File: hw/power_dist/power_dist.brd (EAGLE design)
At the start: 80 x 50 mm, 66 parts, among them J1 JST-ZH6SMT_VERT, J2 JST-PH4SMT_VERT, J3 JST-PH5VERT, P1 XT30P, P2 XT30P, P3 XT30P, P4 XT30P, P5 XT30P, P6 XT30P, P7 XT90PW-M, Q1 PSMN4R8-100BSEJ, Q2 PSMN4R8-100BSEJ, Q3 PSMN4R8-100BSEJ, Q4 MF-DSC-SOT233-BSS138, Q5 MF-DSC-SOT233-MMBT3906, U1 MAX15062AATA+T, U2 STM32G474CEU6, U3 LM5066IPMHE/NOPB, U4 TCAN334G

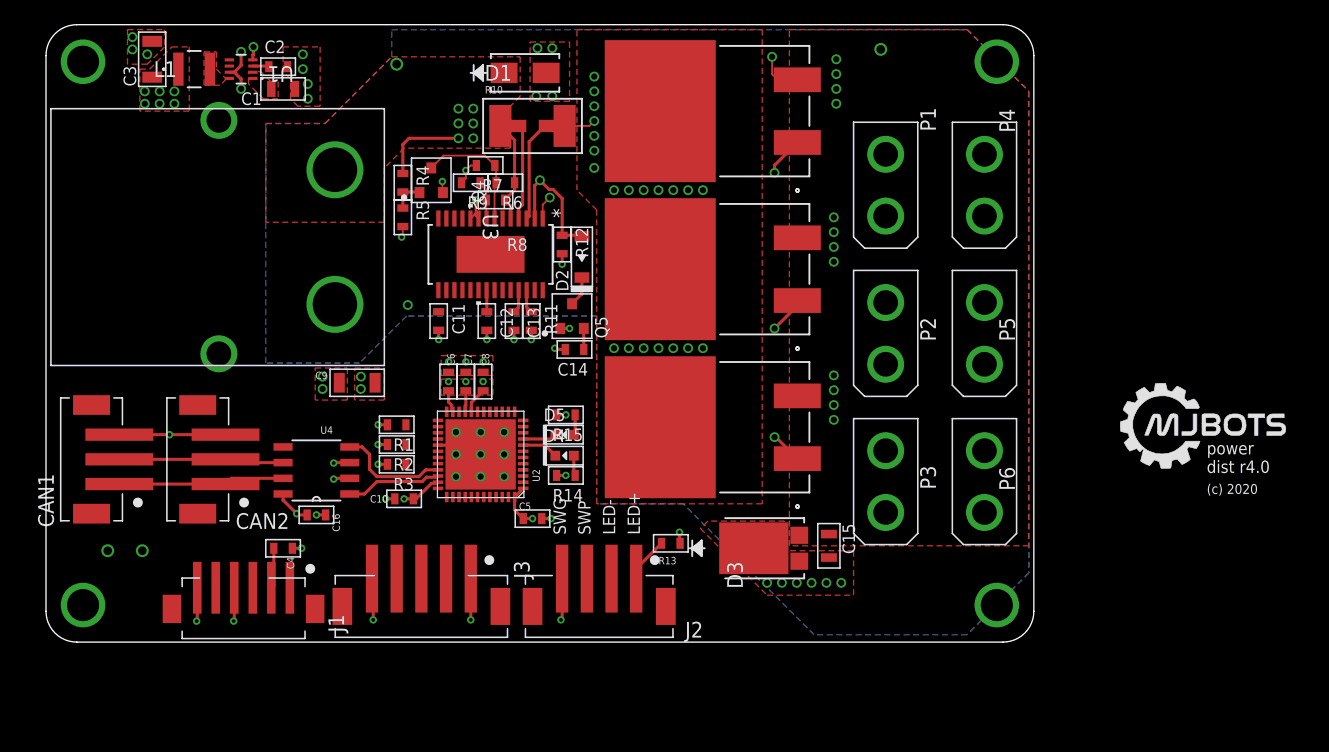
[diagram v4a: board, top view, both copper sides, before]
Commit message: power_dist r4: Resize and rough place silks
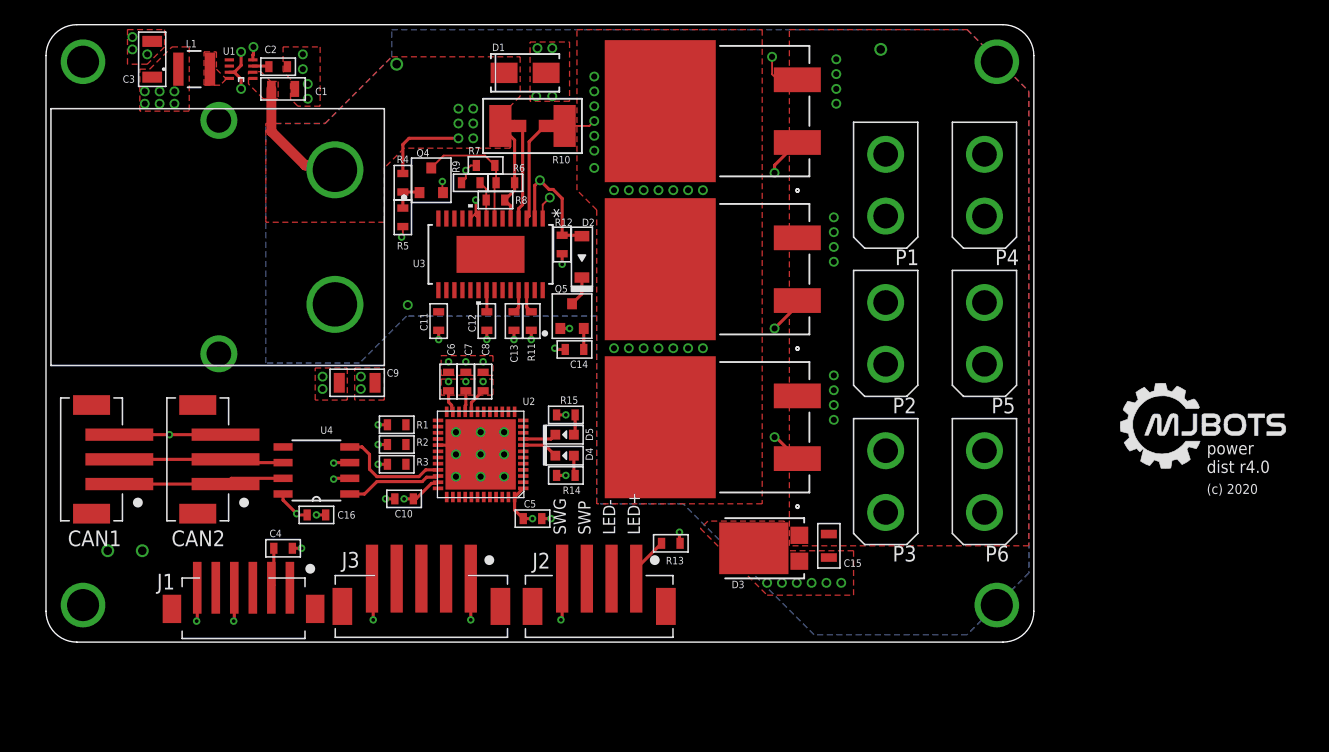
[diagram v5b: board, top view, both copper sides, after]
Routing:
- net +24V: track 15.6 -> 25.4 mm

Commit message: power_dist r4: Place logo
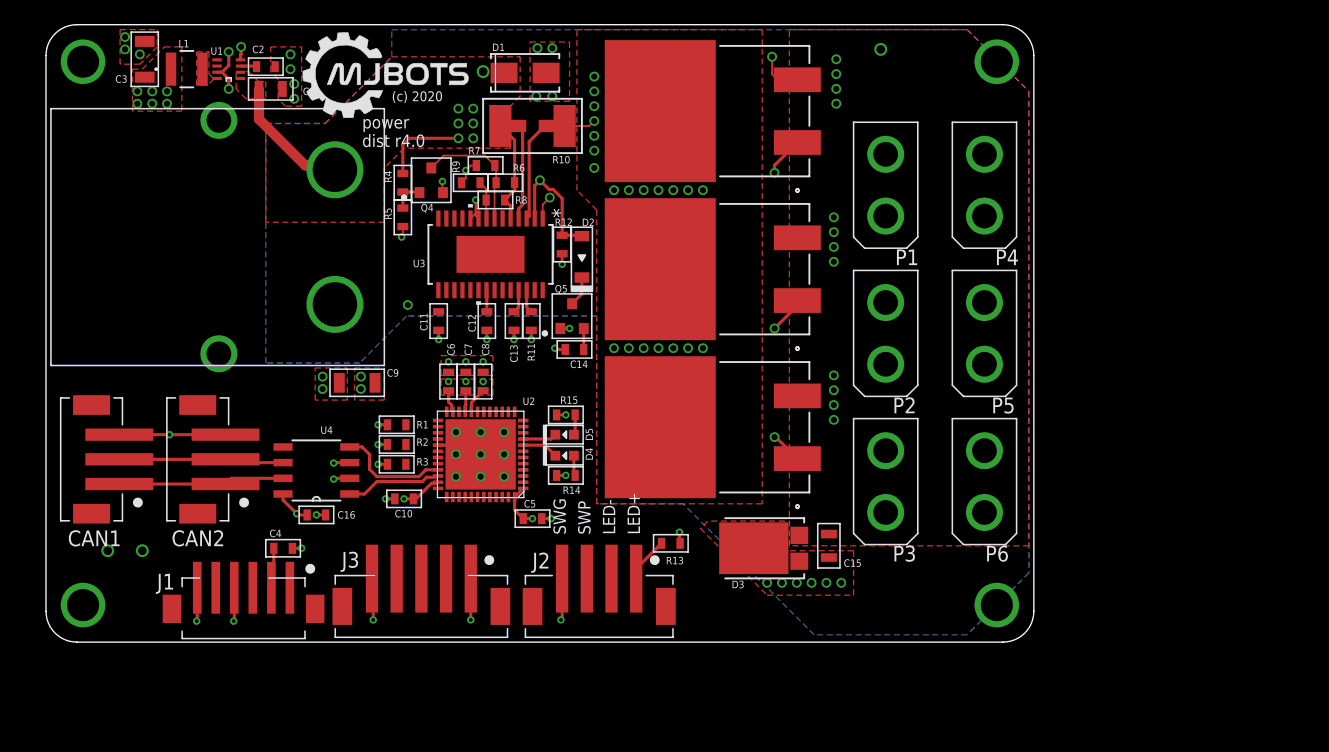
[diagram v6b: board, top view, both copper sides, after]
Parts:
- moved DB_VIN 7.03 mm to (35.4, 46.2)
- moved C1 1.00 mm to (18.2, 44.8)
- moved C2 1.00 mm to (17.8, 46.6)
- moved U1 1.00 mm to (14.8, 46.4)
- moved C3 0.60 mm to (8.00, 47.2)
- moved L1 0.60 mm to (11.4, 46.4)

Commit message: power_dist r4: Routed and labels
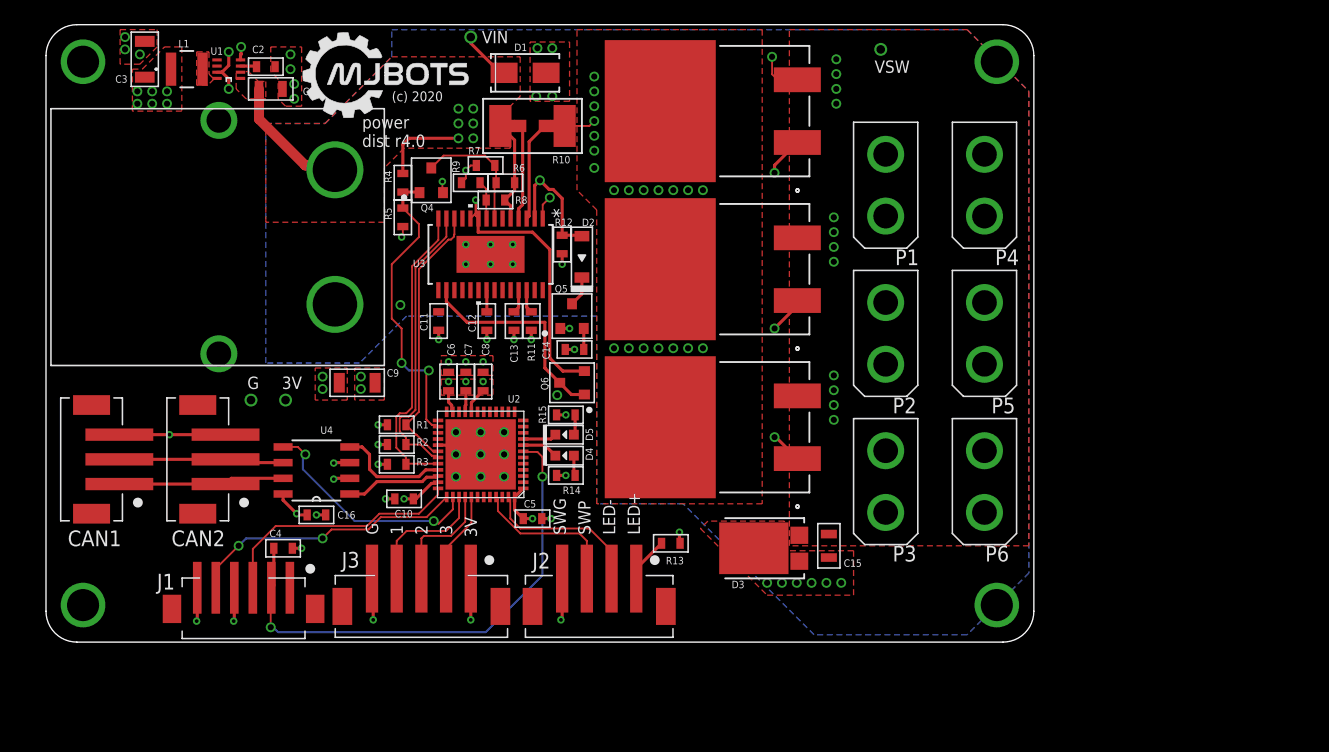
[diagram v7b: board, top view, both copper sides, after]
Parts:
- added Q6: MF-DSC-SOT233-MMBT3904, mfdiscretesemi:SOT-23-3
- moved DB_3 18.9 mm to (19.4, 19.6)
- moved DB_G 15.0 mm to (16.6, 19.6)
- moved DB_VIN 2.97 mm to (34.4, 49.0)
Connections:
- new net N$3: Q6.P$1, Q6.P$3, U3.16
- net CAN_SHDN: now also U2.38; no longer U2.27
- net GND: now also Q6.P$2
- net PWR_LED: now also U2.47; no longer U2.10
- net PWR_SW: now also U2.45; no longer U2.11
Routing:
- net NRST: track 3.28 -> 41.9 mm, vias 0 -> 2
- net SMBA: track 0.00 -> 24.6 mm
- net SCL: track 0.00 -> 23.5 mm
- net SWCLK: track 0.00 -> 22.7 mm, vias 0 -> 2
- net PSHDN: track 2.74 -> 24.9 mm, vias 0 -> 2
- net SDA: track 0.00 -> 21.9 mm
- net SWDIO: track 0.00 -> 20.5 mm
- net GND: track 43.0 -> 62.3 mm, vias 54 -> 60
- net CAN_SHDN: track 0.00 -> 18.8 mm, vias 0 -> 2
- net N$3: track 0.00 -> 17.4 mm
- net PWR_LED: track 0.00 -> 13.3 mm
- net PWR_SW: track 0.00 -> 12.5 mm
- net GPIO1: track 0.00 -> 10.6 mm
- net GPIO2: track 0.00 -> 9.37 mm
- net GPIO3: track 0.00 -> 7.46 mm
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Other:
- board text added: "1"
- board text added: "2"
- board text added: "3"
- board text added: "3V"
- board text added: "G"
- board text added: "VIN"
- board text added: "VSW"

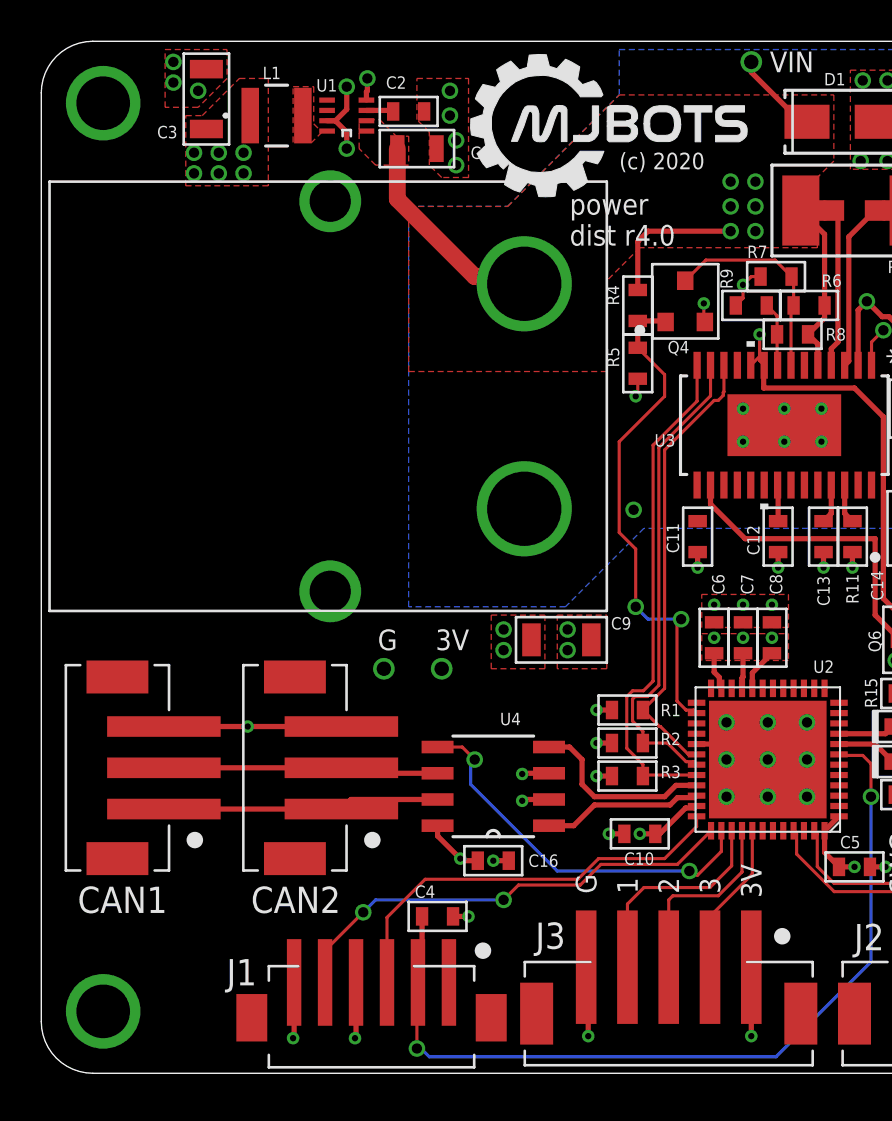
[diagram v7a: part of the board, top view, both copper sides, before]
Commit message: power_dist r4: Optionally ground one of the mounting holes
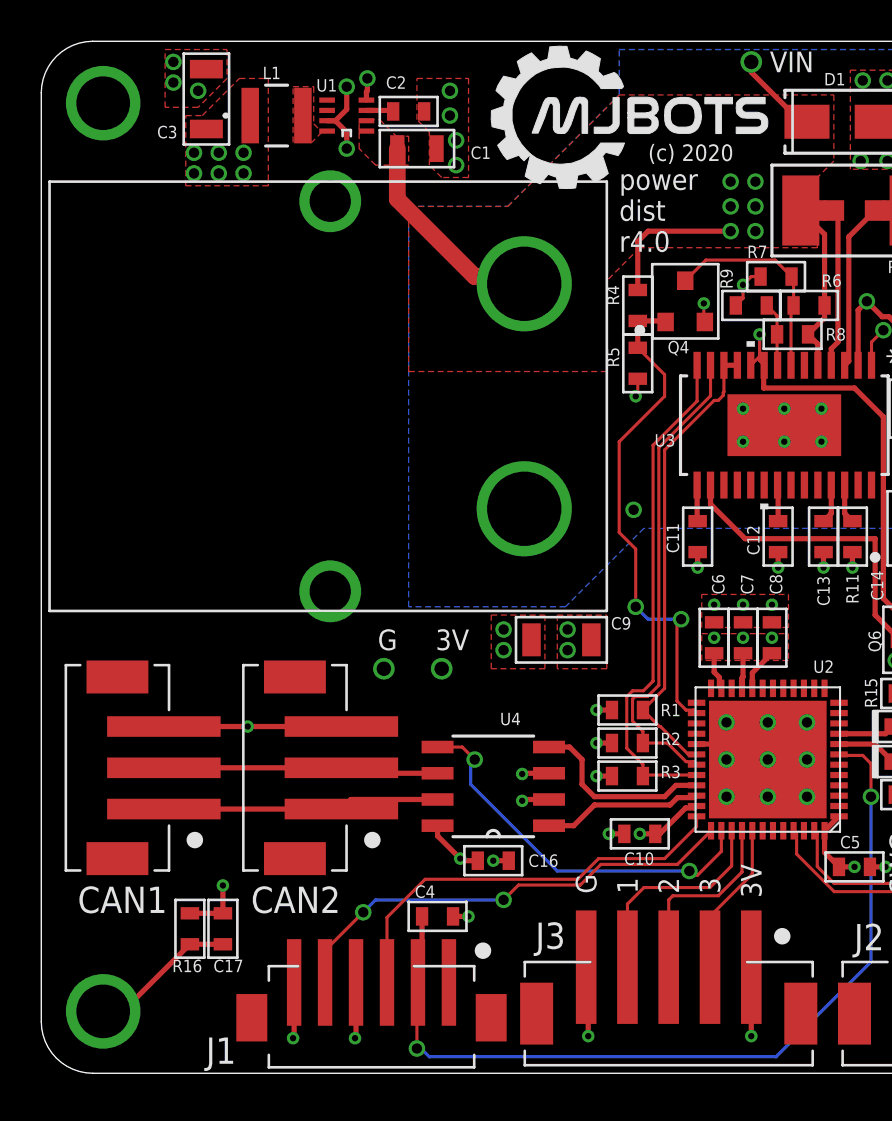
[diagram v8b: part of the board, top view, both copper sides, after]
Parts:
- added C17: DNP, mfpassives:C0603
- added R16: DNP, mfpassives:R0603
- U$1, U$2, U$3, U$4: device precharge:M2.5MOUNT -> power_dist:M2.5MOUNT
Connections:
- new net N$15: C17.P$1, R16.P$1, U$3.P$1
- net GND: now also C17.P$2, R16.P$2
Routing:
- net N$15: track 0.00 -> 7.15 mm
- net GND: track 62.3 -> 65.3 mm, vias 60 -> 61
- net N$7: track 0.00 -> 1.76 mm
- net SDA: track 21.9 -> 22.6 mm
